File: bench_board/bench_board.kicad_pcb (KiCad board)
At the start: 4 copper layers, 80 x 60 mm, 65 parts, among them J1 BATT_4S, J10 BUZZER, J2 BOOT0_JUMPER, J3 USB-C, J4 CRSF_UART, J5 DSHOT_M1-M4, J6 SWD, J7 RX_PWR_5V, J8 TELEM_TX, J9 EXPANSION_BUS, Q1 AO3400A, U1 STM32F405RGT6, U2 TPS54336ADDA, U4 MPU-6000, U5 USBLC6-2SC6, U6 MT3608, Y1 8MHz

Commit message: C23: 7.5nF -> 8.2nF (LCSC C107032) per ngspice loop-gain study; ERC 0, guard 53/2/93
8.2nF raises phase margin at both corners (+1.2 deg at 14.8V and 25.2V)
where 6.8nF lowers it; crossover unchanged within 0.5%. JLCPCB stocks no
7.5nF MLCC. Study harness and results in sim/. Board+schematic value
edited together; guard re-run PASS 53/2/93, ERC 0 violations.

Co-Authored-By: Claude Fable 5 <noreply@anthropic.com>
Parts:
- C23: value 7.5nF -> 8.2nF
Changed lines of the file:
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@@
 			)
 		)
-		(property "Value" "7.5nF"
+		(property "Value" "8.2nF"
 			(at 0 1.16 0)
 			(layer "F.Fab")

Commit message: Batch 6 review fixes: the bench fix that could not be performed, and seven more
Independent review (fresh agent, read-only) returned 1 BLOCKER, 3 HIGH,
6 MEDIUM, 6 LOW. Acted on here:

- BLOCKER: order sheet's 'sub-millimetre solder bridges' for the two
  remaining unconnected pads misread the DRC track-LENGTH field as a
  gap. Re-measured from the board file: U4.1->U4.18 is 3.9mm, U1.48->
  C20.2 is 7.4mm. Remediation rewritten as wire jumpers with routes,
  wire spec, and honest time budget; misread acknowledged in place.
- HIGH: C24.1 removed from the mandatory via-in-pad remark (reviewer
  re-derivation with exact roundrect geometry: nearest via clears by
  0.153mm; false positive). C2.1 near-tangent (0.014mm) added instead.
- HIGH: check_cpl.py default FABDIR and the falsifiability cpl case
  pointed at 17c (were validating the superseded 17b); both re-run,
  PASS/exit 0.
- HIGH: README gate numbers corrected (assembly rows without LCSC
  8->0, not 9->3).
- MEDIUM: board via-protection metadata set (capping yes)(filling yes)
  to match the mandatory fab spec; guard PASS 53/2/93 unchanged.
- MEDIUM: SPICE harness header's wrong PM formula (180-|phase|)
  replaced with the corrected convention note; the study script was
  already right.
- MEDIUM: the 'no 7.5nF at JLCPCB' premise was FALSE as stated -- two
  C0G parts exist in 0603/0805, none in 0402. Corrected in the study
  output, script, and BOM; committed evidence in
  sim/c23_jlcpcb_7p5nF_search.txt; empty _mlcc_head.csv removed. The
  8.2nF choice stands on measured margin + avoided footprint edit.
- MEDIUM: L1/L2 and Y1 verify-before-paying checks surfaced in the
  order sheet's matching step.
- Counts/typos: 51 placed parts, 11 Extended numbers (3), copper-
  edge 0.269/0.298mm, C1 CPL value X7S (board+sch edited, ERC 0,
  guard PASS, CPL/BOM/DRC regenerated, check_cpl PASS).

Not changed, documented as accepted: min_through_hole_diameter 0.15
now also floors component PTH holes (finding 9); guard remains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
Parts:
- C1: value 10uF 50V X7R 1210 -> 10uF 50V X7S 1210
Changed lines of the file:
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@@
 			(back no)
 		)
-		(capping no)
-		(filling no)
+		(capping yes)
+		(filling yes)
 		(pcbplotparams
 			(layerselection 0x00000000_00000000_55555555_5755f5ff)
@@
 			)
 		)
-		(property "Value" "10uF 50V X7R 1210"
+		(property "Value" "10uF 50V X7S 1210"
 			(at 0 2.3 0)
 			(layer "F.Fab")

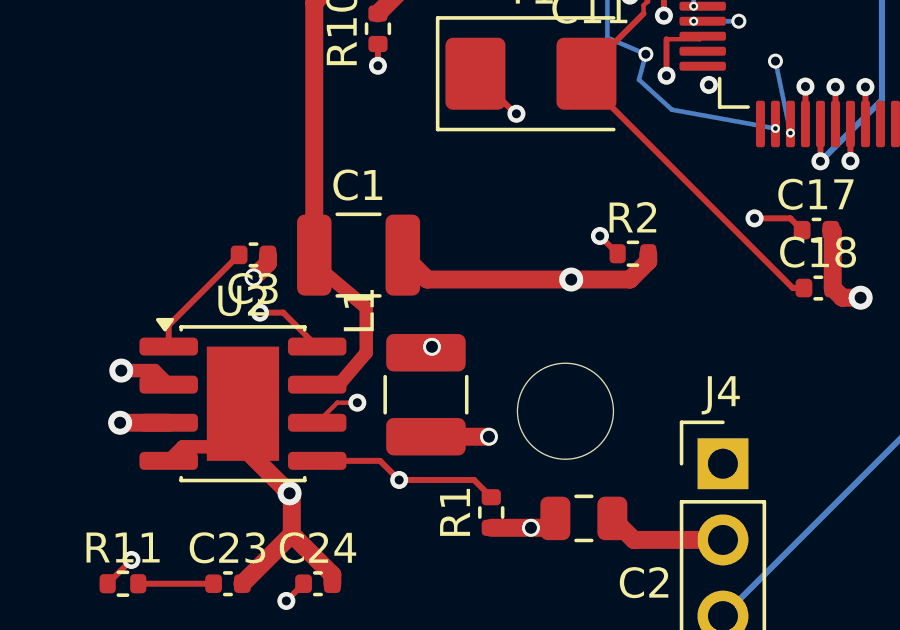
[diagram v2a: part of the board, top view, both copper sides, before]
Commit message: Item 1: EN abs-max violation fixed -- TI Figure-15 UVLO divider, EN never above 2.6V
THE ARITHMETIC (from SLVSCD5D Eq. 2/3 with the device's own numbers:
Ip=1.15uA, Ih=3.3uA, VENrising=1.21V, VENfalling=1.17V):
targets Vstart=12.0V, Vstop=11.0V give R1=180.74k, R2=19.89k exact;
fitted E96 pair R16=182k (LCSC C11481, Extended -- no Basic exists at
180k/182k 0402), R17=20k (C25765, Basic). Realized thresholds:
  START (rising)  = 1.21*(1+182/20) - 1.15uA*182k = 12.012V (3.003V/cell)
  STOP  (falling) = 1.17*(1+182/20) - 4.45uA*182k = 11.007V (2.752V/cell)
  hysteresis 1.005V (datasheet recommends >500mV)
EN pin voltage (divider + (Ip+Ih)*R1||R2): 1.27V @12V, 1.74V @16.8V,
2.58V @25.2V -- all far under the 6V abs-max at every corner including
6S. Idle divider drain 83uA from the pack.

Schematic: EN label on U2.7 renamed to EN_UVLO; R16 VBAT_4S->EN_UVLO,
R17 EN_UVLO->GND; ERC 0. Netlist verified: /EN_UVLO = {U2.7, R16.2,
R17.1} exactly; EN removed from /VBAT_4S.

Board: old EN spur (4 segments C1.1 -> pad 7) deleted; R16/R17 placed
at (21.25,41.85)/(23.15,41.7) in the strip south of C1; VBAT tap into
C1.1; EN runs R16.P2 -> short F.Cu stub -> B.Cu (empty there) ->
via -> F.Cu -> U2.7, dodging the COMP via, L1 pads, and MH3's 6mm
mask aperture (an F.Cu corner at (21.8,44.7) turned out to poke 0.15mm
into that aperture and lit up 6 solder-mask-bridge violations -- the
B.Cu detour exists because F.Cu is walled by the GND highway at
y=40.86, C1, L1, and that aperture). R17 GND taps the existing 0.6mm
GND trace at y=40.86 -- no new GND via needed. Two new 0.6/0.3 EN
vias; the one at (21.76,42.1) overlaps R16's own EN pad edge -- add it
to the filled-and-capped list.

Guard: 53 violations / 2 unconnected / 95 parity. Violations AT
baseline; unconnected = the two known bench-jumper pads; parity +2 is
exactly the two new footprints' empty-field mismatches (same class as
the existing 61). Baseline re-recorded at 53/2/95 with this
justification. Planes refilled with KiCad's own 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
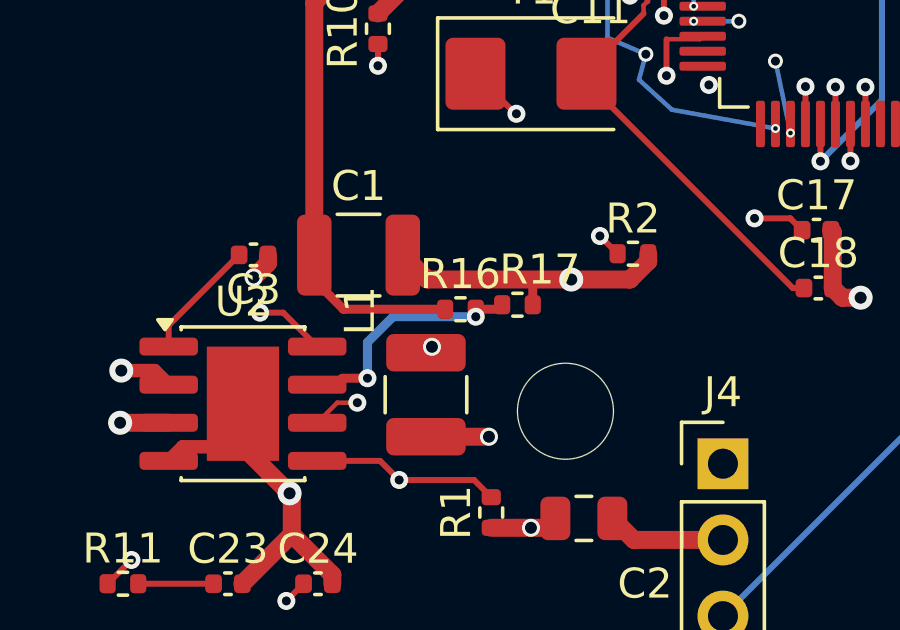
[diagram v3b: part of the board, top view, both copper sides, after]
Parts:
- added R16: 182k, Resistor_SMD:R_0402_1005Metric, F.Cu at (21.2, 41.9)
- added R17: 20k, Resistor_SMD:R_0402_1005Metric, F.Cu at (23.1, 41.7)
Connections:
- U2 pad 7: /VBAT_4S -> /EN_UVLO
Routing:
- net /EN_UVLO: track 0.00 -> 7.14 mm, vias 0 -> 2
- net /VBAT_4S: track 47.7 -> 46.1 mm
- net /GND: track 134.8 -> 135.4 mm

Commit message: Item 2: MPU-6000 charge-pump cap fixed on all three axes -- 2.2nF, 50V part, returned to GND
Per PS-MPU-6000A section 7.3: CPOUT capacitor must be 2.2nF X7R 50V to
GND; the board had 100nF/16V to 3V3. Schematic: C20 pin-2 label 3V3 ->
GND, value 100nF -> 2.2nF; ERC 0; netlist verified /MPU_CPOUT =
{C20.1, U4.20} and C20.2 now in /GND. Part: Yageo CC0402KRX7R9BB222,
LCSC C106861 (X7R 50V, 1.14M stock) -- no Basic-library 2.2nF/50V 0402
exists, so this is one more Extended fee, said plainly.

Board: pad 2 renet to /GND; the two 3V3 feeder segments deleted (C21.1
keeps its feed from the far side -- verified the chain is fed from
(44.708,34.932), not through C20); new 0.3mm GND return east-then-north
to the existing 0.8/0.4 GND via at (45.753,29.452), dodging C20's own
CPOUT pad (first attempt clipped it at 0.17mm -- caught by the guard,
rerouted) and the CPOUT via. No new vias.

CONSEQUENCE FOR THE ORDER SHEET (picked up in item 4): the U1.48 bench
jumper's documented target was C20 pad 2 *because it was 3V3*. It is
GND now. New target: C21 pad 1 (45.599,34.041), /3V3, 9.2mm from pad
48.

Guard: PASS 53/2/95, unchanged from the item-1 baseline. Planes
refilled, 4/4 coherent.

Co-Authored-By: Claude Fable 5 <noreply@anthropic.com>
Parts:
- C20: value 100nF -> 2.2nF
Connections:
- C20 pad 2: /3V3 -> /GND
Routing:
- net /GND: track 135.4 -> 139.3 mm
- net /3V3: track 57.4 -> 55.3 mm
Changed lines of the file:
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@@
 			)
 		)
-		(property "Value" "100nF"
+		(property "Value" "2.2nF"
 			(at 0 1.16 270)
 			(layer "F.Fab")
@@
 			(layers "F.Cu" "F.Mask" "F.Paste")
 			(roundrect_rratio 0.25)
-			(net "/3V3")
+			(net "/GND")
 		)
 		(embedded_fonts no)
@@
 	)
 	(segment
+		(start 17.35 41.85)
+		(end 16.75 41.25)
+		(width 0.3)
+		(layer "F.Cu")
+		(net "/VBAT_4S")
+	)
+	(segment
+		(start 11.0558 43.8958)
+		(end 11.525 44.365)
+		(width 0.45)
+		(layer "F.Cu")
+		(net "/VBAT_4S")
+	)
+	(segment
+		(start 17.7968 30.2132)
+		(end 18.5 29.51)
+		(width 0.6)
+		(layer "F.Cu")
+		(net "/VBAT_4S")
+	)
+	(segment
+		(start 16.378 31.632)
+		(end 16.378 40.046)
+		(width 0.6)
+		(layer "F.Cu")
+		(net "/VBAT_4S")
+	)
+	(segment
+		(start 16.378 40.046)
+		(end 16.378 40.3428)
+		(width 0.6)
+		(layer "F.Cu")
+		(net "/VBAT_4S")
+	)
+	(segment
+		(start 17.7968 30.2132)
+		(end 16.378 31.632)
+		(width 0.6)
+		(layer "F.Cu")
+		(net "/VBAT_4S")
+	)
+	(segment
+		(start 9.9446 43.8958)
+		(end 11.0558 43.8958)
+		(width 0.45)
+		(layer "F.Cu")
+		(net "/VBAT_4S")
+	)
+	(segment
+		(start 20.74 41.85)
+		(end 17.35 41.85)
+		(width 0.3)
+		(layer "F.Cu")
+		(net "/VBAT_4S")
+	)
+	(via
+		(at 9.9446 43.8958)
+		(size 0.8)
+		(drill 0.4)
+		(layers "F.Cu" "B.Cu")
+		(net "/VBAT_4S")
+	)
+	(via
+		(at 17.7968 30.2132)
+		(size 0.8)
+		(drill 0.4)
+		(layers "F.Cu" "B.Cu")
+		(net "/VBAT_4S")
+	)
+	(segment
+		(start 9.9446 43.8958)
+		(end 6 39.9512)
+		(width 0.6)
+		(layer "In1.Cu")
+		(net "/VBAT_4S")
+	)
+	(segment
+		(start 6 39.9512)
+		(end 6 30)
+		(width 0.6)
+		(layer "In1.Cu")
+		(net "/VBAT_4S")
+	)
+	(segment
+		(start 17.7968 30.2132)
+		(end 16.6583 31.3517)
+		(width 0.6)
+		(layer "In2.Cu")
+		(net "/VBAT_4S")
+	)
+	(segment
+		(start 7.3517 31.3517)
+		(end 6 30)
+		(width 0.6)
+		(layer "In2.Cu")
+		(net "/VBAT_4S")
+	)
+	(segment
+		(start 16.6583 31.3517)
+		(end 7.3517 31.3517)
+		(width 0.6)
+		(layer "In2.Cu")
+		(net "/VBAT_4S")
+	)
+	(segment
+		(start 21.76 41.85)
+		(end 21.76 42.1)
+		(width 0.3)
+		(layer "F.Cu")
+		(net "/EN_UVLO")
+	)
+	(segment
+		(start 21.76 41.85)
+		(end 22.64 41.85)
+		(width 0.3)
+		(layer "F.Cu")
+		(net "/EN_UVLO")
+	)
+	(segment
+		(start 18.15 44.15)
+		(end 17.3 44.15)
+		(width 0.3)
+		(layer "F.Cu")
+		(net "/EN_UVLO")
+	)
+	(via
+		(at 21.76 42.1)
+		(size 0.6)
+		(drill 0.3)
+		(layers "F.Cu" "B.Cu")
+		(net "/EN_UVLO")
+	)
+	(via
+		(at 18.15 44.15)
+		(size 0.6)
+		(drill 0.3)
+		(layers "F.Cu" "B.Cu")
+		(net "/EN_UVLO")
+	)
+	(segment
+		(start 21.76 42.1)
+		(end 19 42.1)
+		(width 0.3)
+		(layer "B.Cu")
+		(net "/EN_UVLO")
+	)
+	(segment
+		(start 18.15 42.95)
+		(end 18.15 44.15)
+		(width 0.3)
+		(layer "B.Cu")
+		(net "/EN_UVLO")
+	)
+	(segment
+		(start 19 42.1)
+		(end 18.15 42.95)
+		(width 0.3)
+		(layer "B.Cu")
+		(net "/EN_UVLO")
+	)
+	(segment
 		(start 54.01 29.5)
 		(end 54.5917 30.0817)
@@
 	)
 	(segment
-		(start 45.095 32.187)
-		(end 45.599 32.691)
-		(width 0.6)
-		(layer "F.Cu")
-		(net "/3V3")
-	)
-	(segment
 		(start 36.985 39.819)
 		(end 37.9761 38.8279)
@@
 	)
 	(segment
-		(start 45.599 32.691)
-		(end 45.599 34.041)
-		(width 0.6)
-		(layer "F.Cu")
-		(net "/3V3")
-	)
-	(segment
 		(start 38.75 35.675)
 		(end 42.3927 36.757)
@@
 	)
 	(segment
+		(start 46.35 30.049)
+		(end 45.753 29.452)
+		(width 0.3)
+		(layer "F.Cu")
+		(net "/GND")
+	)
+	(segment
 		(start 5.7133 8.1492)
 		(end 5.8625 8)
@@
 	)
 	(segment
-		(start 17.35 41.85)
-		(end 16.75 41.25)
-		(width 0.3)
-		(layer "F.Cu")
-		(net "/VBAT_4S")
-	)
-	(segment
-		(start 11.0558 43.8958)
-		(end 11.525 44.365)
-		(width 0.45)
-		(layer "F.Cu")
-		(net "/VBAT_4S")
-	)
-	(segment
-		(start 17.7968 30.2132)
-		(end 18.5 29.51)
-		(width 0.6)
-		(layer "F.Cu")
-		(net "/VBAT_4S")
-	)
-	(segment
-		(start 16.378 31.632)
-		(end 16.378 40.046)
-		(width 0.6)
-		(layer "F.Cu")
-		(net "/VBAT_4S")
-	)
-	(segment
-		(start 16.378 40.046)
-		(end 16.378 40.3428)
-		(width 0.6)
-		(layer "F.Cu")
-		(net "/VBAT_4S")
-	)
-	(segment
-		(start 17.7968 30.2132)
-		(end 16.378 31.632)
-		(width 0.6)
-		(layer "F.Cu")
-		(net "/VBAT_4S")
-	)
-	(segment
-		(start 9.9446 43.8958)
-		(end 11.0558 43.8958)
-		(width 0.45)
-		(layer "F.Cu")
-		(net "/VBAT_4S")
-	)
-	(segment
-		(start 20.74 41.85)
-		(end 17.35 41.85)
-		(width 0.3)
-		(layer "F.Cu")
-		(net "/VBAT_4S")
-	)
-	(via
-		(at 9.9446 43.8958)
-		(size 0.8)
-		(drill 0.4)
-		(layers "F.Cu" "B.Cu")
-		(net "/VBAT_4S")
-	)
-	(via
-		(at 17.7968 30.2132)
-		(size 0.8)
-		(drill 0.4)
-		(layers "F.Cu" "B.Cu")
-		(net "/VBAT_4S")
-	)
-	(segment
-		(start 9.9446 43.8958)
-		(end 6 39.9512)
-		(width 0.6)
-		(layer "In1.Cu")
-		(net "/VBAT_4S")
-	)
-	(segment
-		(start 6 39.9512)
-		(end 6 30)
-		(width 0.6)
-		(layer "In1.Cu")
-		(net "/VBAT_4S")
-	)
-	(segment
-		(start 17.7968 30.2132)
-		(end 16.6583 31.3517)
-		(width 0.6)
-		(layer "In2.Cu")
-		(net "/VBAT_4S")
-	)
-	(segment
-		(start 7.3517 31.3517)
-		(end 6 30)
-		(width 0.6)
-		(layer "In2.Cu")
-		(net "/VBAT_4S")
-	)
-	(segment
-		(start 16.6583 31.3517)
-		(end 7.3517 31.3517)
-		(width 0.6)
-		(layer "In2.Cu")
-		(net "/VBAT_4S")
-	)
-	(segment
 		(start 45.5 51)
 		(end 46.49 51)
@@
 	)
 	(segment
-		(start 21.76 41.85)
-		(end 21.76 42.1)
-		(width 0.3)
-		(layer "F.Cu")
-		(net "/EN_UVLO")
-	)
-	(segment
-		(start 21.76 41.85)
-		(end 22.64 41.85)
-		(width 0.3)
-		(layer "F.Cu")
-		(net "/EN_UVLO")
-	)
-	(segment
-		(start 18.15 44.15)
-		(end 17.3 44.15)
-		(width 0.3)
-		(layer "F.Cu")
-		(net "/EN_UVLO")
-	)
-	(via
-		(at 21.76 42.1)
-		(size 0.6)
-		(drill 0.3)
-		(layers "F.Cu" "B.Cu")
-		(net "/EN_UVLO")
-	)
-	(via
-		(at 18.15 44.15)
-		(size 0.6)
-		(drill 0.3)
-		(layers "F.Cu" "B.Cu")
-		(net "/EN_UVLO")
-	)
-	(segment
-		(start 21.76 42.1)
-		(end 19 42.1)
-		(width 0.3)
-		(layer "B.Cu")
-		(net "/EN_UVLO")
-	)
-	(segment
-		(start 18.15 42.95)
-		(end 18.15 44.15)
-		(width 0.3)
-		(layer "B.Cu")
-		(net "/EN_UVLO")
-	)
-	(segment
-		(start 19 42.1)
-		(end 18.15 42.95)
-		(width 0.3)
-		(layer "B.Cu")
-		(net "/EN_UVLO")
-	)
-	(segment
 		(start 15.4461 51.5739)
 		(end 16.02 51)
@@
 		(net "/USB_DP_MCU")
 	)
+	(segment
+		(start 45.095 32.187)
+		(end 45.75 32.187)
+		(width 0.3)
+		(layer "F.Cu")
+		(net "/GND")
+	)
+	(segment
+		(start 45.75 32.187)
+		(end 46.35 31.587)
+		(width 0.3)
+		(layer "F.Cu")
+		(net "/GND")
+	)
+	(segment
+		(start 46.35 31.587)
+		(end 46.35 30.049)
+		(width 0.3)
+		(layer "F.Cu")
+		(net "/GND")
+	)
 	(zone

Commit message: Item 3: crystal load caps C17/C18 10pF -> 33pF (CL=20pF crystal, manufacturer-confirmed)
Y1 (C115962, YXC X50328MSB2GI) is a 20pF-load crystal per the Yangxing
spec sheet read in the 2026-08-18 datasheet pass. 33pF gives
CL = 33/2 + ~3 stray = 19.5pF against the 20pF spec; the previous 10pF
pair ran the oscillator at ~8pF, ~+200-350ppm fast. Part: FH
0402CG330J500NT, LCSC C1562, C0G 50V, Basic library, 690k stock -- C0G
is also the right dielectric for load caps. Value-only change,
schematic and board together; ERC 0; guard PASS 53/2/95 unchanged.

C1 confirmed carried: schematic/board value still '10uF 50V X7S 1210'
(GCM32EC71H106KA03 / C126612 bias-verified resolution intact).

Co-Authored-By: Claude Fable 5 <noreply@anthropic.com>
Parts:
- C17, C18: value 10pF -> 33pF
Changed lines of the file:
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@@
 			)
 		)
-		(property "Value" "10pF"
+		(property "Value" "33pF"
 			(at 0 1.16 0)
 			(layer "F.Fab")
@@
 			)
 		)
-		(property "Value" "10pF"
+		(property "Value" "33pF"
 			(at 0 1.16 0)
 			(layer "F.Fab")
